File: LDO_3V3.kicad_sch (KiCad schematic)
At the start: 7 parts, among them U4 TPS7A8101DRBR

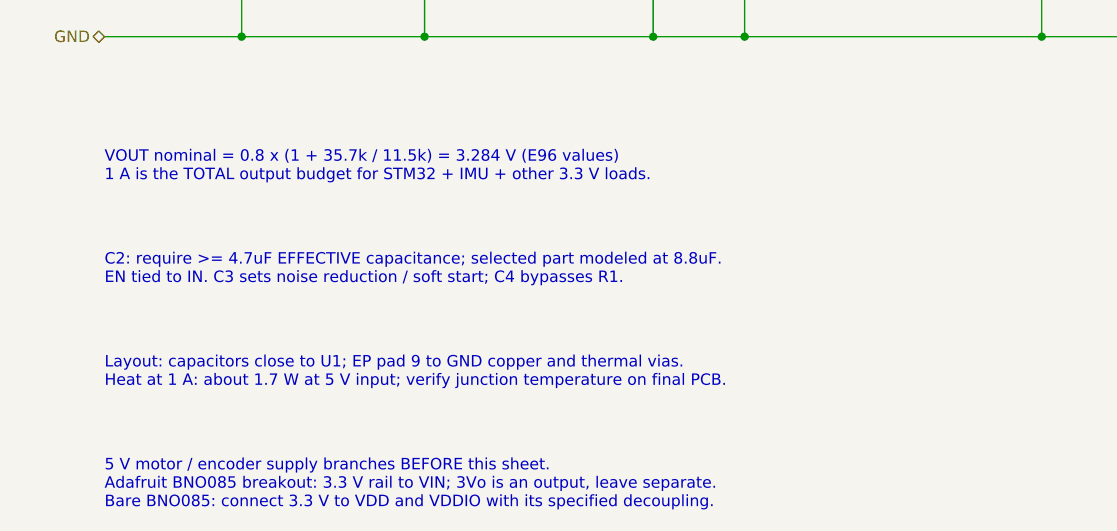
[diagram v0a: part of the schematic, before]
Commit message: Remove the IMU from the board; it will be wired off-board
The BNO085 IMU is now connected discretely off the PCB, so everything
for it is removed from the schematic and the layout:
- Delete the IMU Interface sheet (IMU_Interface.kicad_sch): J11 STEMMA
  QT connector, J12 INT/RST header, DNP I2C pull-ups R10/R11 and series
  resistors R34/R35; remove its sheet block, note and project entry
- Remove debug LED D10 / R23 (LED_IMU on PB13)
- Rename the freed MCU nets back to plain pins, still broken out on the
  GPIO headers: IMU_SCL -> PB6, IMU_SDA -> PB7 (J9), IMU_INT -> PC4,
  IMU_RST -> PC5 (J10), LED_IMU -> PB13 (J9)
- Drop IMU wiring notes and the IMU 3.3 V budget line from the LDO sheet;
  update the J9/J10 pin descriptions, debug-LED note and README

Board updated to match (as Update PCB from Schematic): the eight
unplaced footprints deleted, pad nets renamed, J9/J10 descriptions
synced. ERC 0; DRC unchanged at 57 with 276 unrouted (was 293);
schematic parity clean.

Co-Authored-By: Claude Opus 5.5 <noreply@anthropic.com>
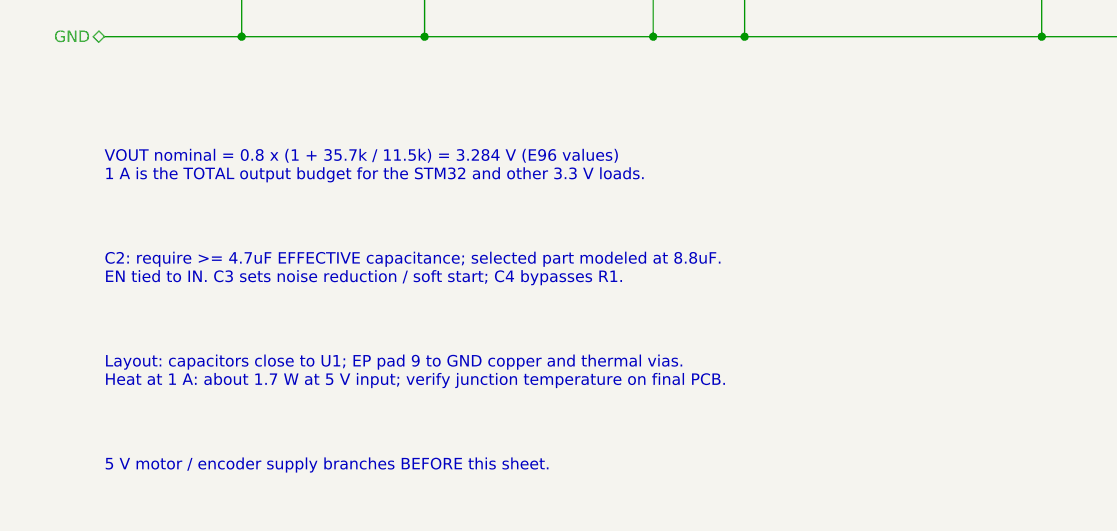
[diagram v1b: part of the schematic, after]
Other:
- note added: "5 V motor / encoder supply branches BEFORE this sheet."
- note added: "VOUT nominal = 0.8 x (1 + 35.7k / 11.5k) = 3.284 V (E96 values) 1 A is the TOTAL output budget for the STM32 and other 3.3 V loads."
- note removed: "5 V motor / encoder supply branches BEFORE this sheet. Adafruit BNO085 breakout: 3.3 V rail to VIN; 3Vo is an output, leave separate. Bare BNO085: connect 3.3 V to VDD and VDDIO with its specified decoupling."
- note removed: "VOUT nominal = 0.8 x (1 + 35.7k / 11.5k) = 3.284 V (E96 values) 1 A is the TOTAL output budget for STM32 + IMU + other 3.3 V loads."
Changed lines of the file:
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@@
 		(comment 1 "5 V to 3.3 V, 1 A total rail capacity")
 	)
-	(text "VOUT nominal = 0.8 x (1 + 35.7k / 11.5k) = 3.284 V (E96 values)\n1 A is the TOTAL output budget for STM32 + IMU + other 3.3 V loads."
+	(text "VOUT nominal = 0.8 x (1 + 35.7k / 11.5k) = 3.284 V (E96 values)\n1 A is the TOTAL output budget for the STM32 and other 3.3 V loads."
 		(exclude_from_sim no)
 		(at 60.96 144.78 0)
@@
 		)
 	)
-	(text "5 V motor / encoder supply branches BEFORE this sheet.\nAdafruit BNO085 breakout: 3.3 V rail to VIN; 3Vo is an output, leave separate.\nBare BNO085: connect 3.3 V to VDD and VDDIO with its specified decoupling."
+	(text "5 V motor / encoder supply branches BEFORE this sheet."
 		(exclude_from_sim no)
 		(at 60.96 179.07 0)

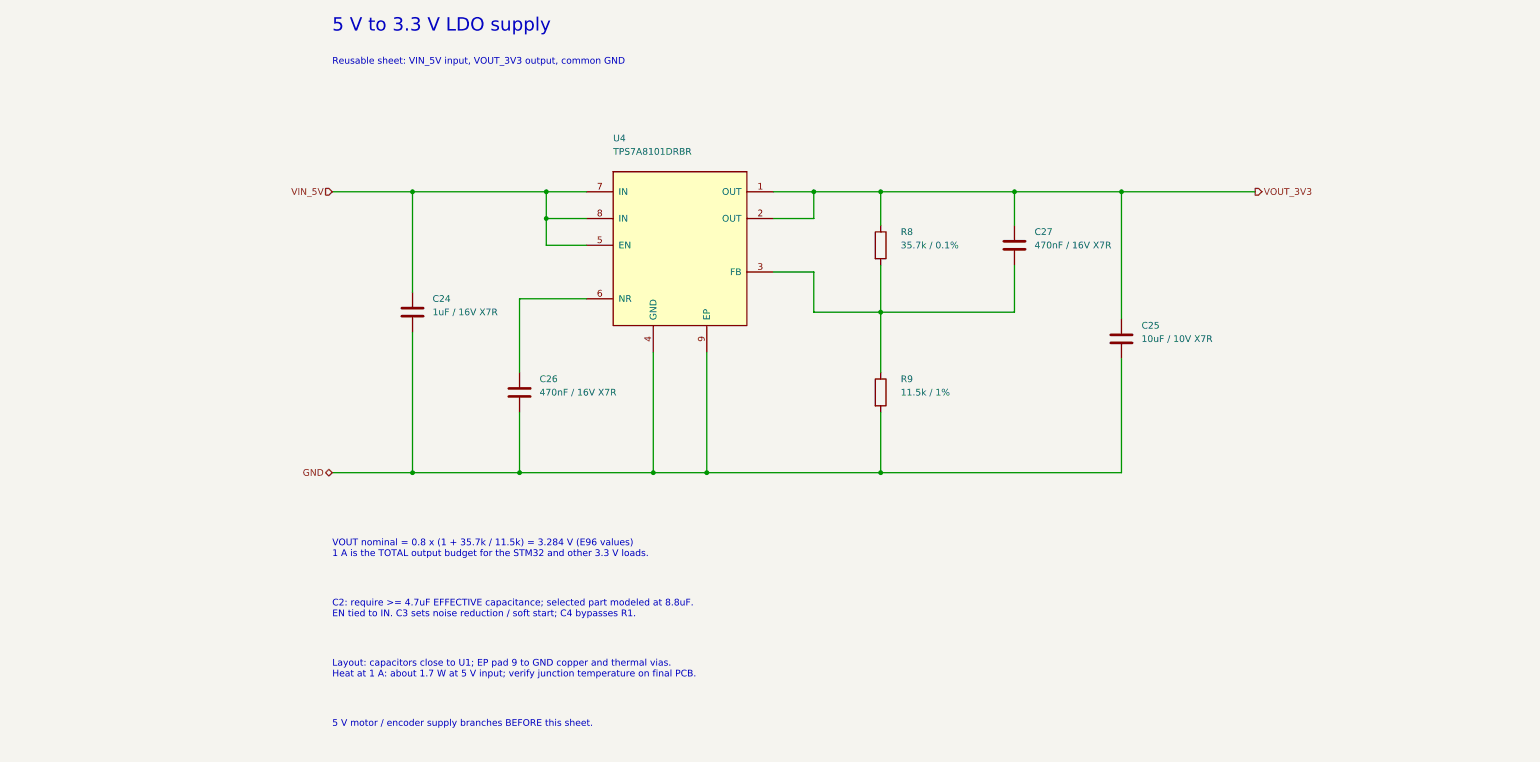
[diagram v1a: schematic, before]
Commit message: Add input protection, AUX ports, servo interface and Pi control
Implements the 2026-10-15 design review decisions in the schematic.
ERC 0 errors, 0 warnings.

New sheets:
- Input Protection: Q1 SQJ409EP reverse-battery P-FET after F1 (D12
  12 V gate clamp, R36), D13 SMBJ16A TVS on +12V, battery sense
  R37/R38/C37 -> VBAT_SENSE on PA0. PWR_FLAG moves to +12V.
- AUX Outputs: four +5V_AUX ports J18-J21 (JST XH 2-pin: Notecard,
  LiDAR, GNSS, IMU), each through a 1.5 A PTC (F4-F7).
- Servo Interface: J17 (GND, VBAT_SERVO via F3 5 A fuse, SERVO_SIG) for
  the Hiwonder HTS-30HS through an external 11.1-12 V buck. U8
  SN74LVC1T45 translates PB10 (USART3 half-duplex) to the 5 V bus,
  PB11 sets direction; R39-R42 pull-ups/series, D14 ESD.

Root sheet:
- F1 output is now VBAT_FUSED; C36 sits on +12V after Q1. J2-F1 net
  named VBAT_IN. F1 7.5 A -> 10 A (0297010.L).
- Y3/C5/C6 fitted (were DNP).
- PA0 -> VBAT_SENSE, PA1 -> PI_3V3_SENSE, PB10 -> SERVO_TX,
  PB11 -> SERVO_DIR. Notes updated (no more F2 / XT30-only text).

Pi 5 Interface:
- J13 -> 6-pin JST XH: TXD, RXD, GND, PI_3V3, PI_RESET, PI_BOOT0.
- PI_3V3 -> D15 -> AUX_EN (U5 enable) and R44/R45 -> PA1.
- PI_RESET -> Q2 DMN63D8L -> NRST (open drain, R46 pull-down).
- PI_BOOT0 -> R47 1k -> BOOT0, for reflashing over USART2.
- R12/R13 100R -> 1k (PA2/PA3 are TTa, 5 mA injection max).
- Remove TP2 (same net as TP1 since F2 was removed).

Buck 5V AUX: U5 EN from AUX_EN (was +12V), R43 100k pull-down, C40,
J22 force-on jumper. Buck 5V SYS: C49 100 nF at U3 VIN/GND.
U2/U5 value TPSM63606RDLR; VCC design note corrected (internal 1 uF,
must stay NC).

Motor Control (now A3):
- U9/U10 74LVC2G17 encoder buffers on +3V3; encoder series R 100R ->
  1k with C43-C46 1 nF; R48-R51 4.7k pull-ups (DNP).
- F8/F9 0.2 A PTC + C47/C48 on each encoder supply (ENC1_5V, ENC2_5V).
- J7/J15 pin order 5V, GND, A, B (matches the am-3651 plug).
- R52/R53 10k pull-downs on both PWM lines (MDD20A brakes on low).
- F10/F11 PTC in series with J6/J16 p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
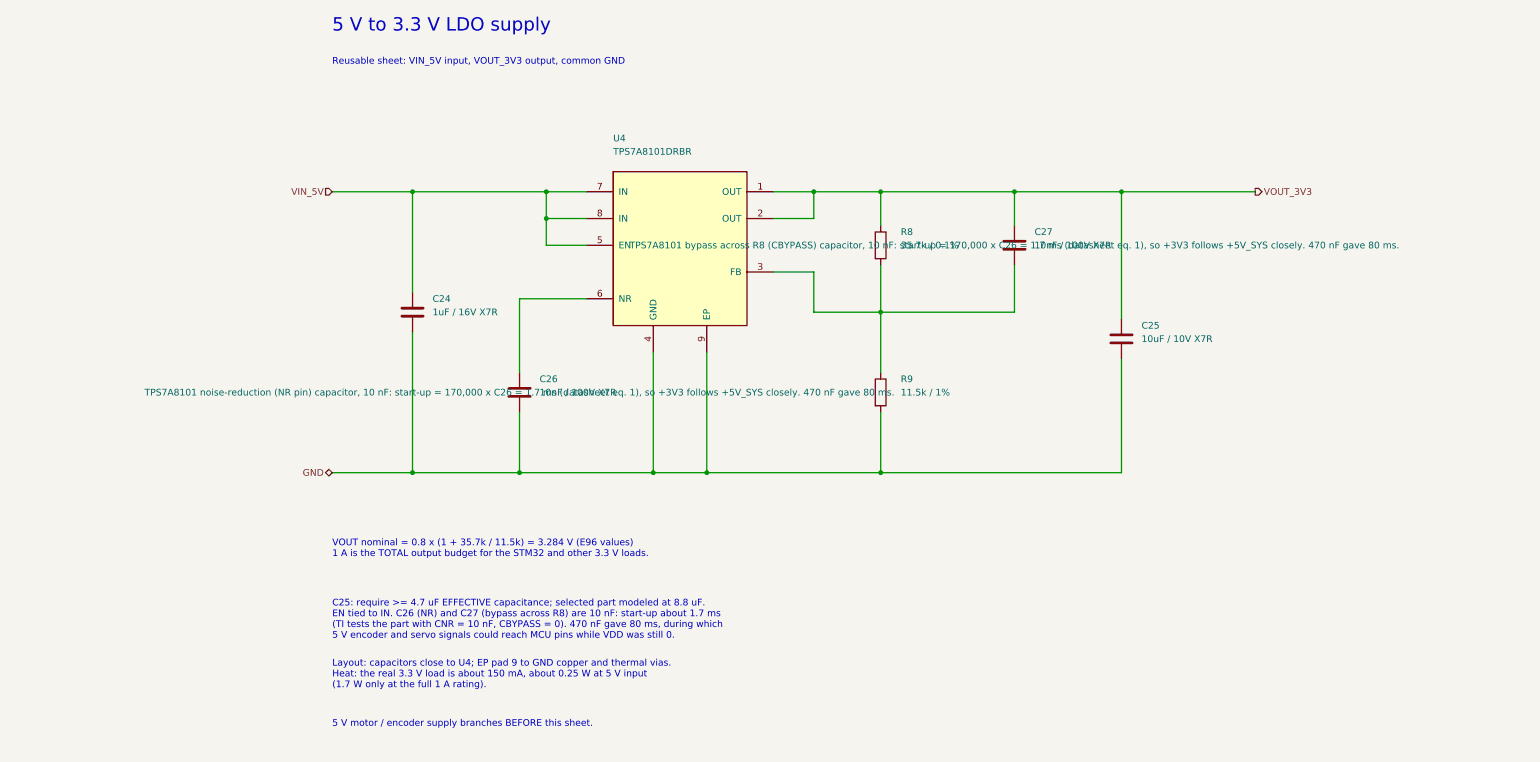
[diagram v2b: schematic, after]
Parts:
- C26, C27: value 470nF / 16V X7R -> 10nF / 100V X7R; MPN GRM188R71C474KA88D -> GRM188R72A103KA01D
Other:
- note added: "C25: require >= 4.7 uF EFFECTIVE capacitance; selected part modeled at 8.8 uF. EN tied to IN. C26 (NR) and C27 (bypass across R8) are 10 nF: start-up about 1.7 ms (TI tests the part with CNR = 10 nF, CBYPASS = 0). 470 nF gave 80 ms, during which 5 V encoder and servo signals could reach MCU pins while VDD was still 0."
- note added: "Layout: capacitors close to U4; EP pad 9 to GND copper and thermal vias. Heat: the real 3.3 V load is about 150 mA, about 0.25 W at 5 V input (1.7 W only at the full 1 A rating)."
- note removed: "C2: require >= 4.7uF EFFECTIVE capacitance; selected part modeled at 8.8uF. EN tied to IN. C3 sets noise reduction / soft start; C4 bypasses R1."
- note removed: "Layout: capacitors close to U1; EP pad 9 to GND copper and thermal vias. Heat at 1 A: about 1.7 W at 5 V input; verify junction temperature on final PCB."
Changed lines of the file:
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@@
 		)
 	)
-	(text "C2: require >= 4.7uF EFFECTIVE capacitance; selected part modeled at 8.8uF.\nEN tied to IN. C3 sets noise reduction / soft start; C4 bypasses R1."
+	(text "C25: require >= 4.7 uF EFFECTIVE capacitance; selected part modeled at 8.8 uF.\nEN tied to IN. C26 (NR) and C27 (bypass across R8) are 10 nF: start-up about 1.7 ms\n(TI tests the part with CNR = 10 nF, CBYPASS = 0). 470 nF gave 80 ms, during which\n5 V encoder and servo signals could reach MCU pins while VDD was still 0."
 		(exclude_from_sim no)
 		(at 60.96 156.21 0)
@@
 		)
 	)
-	(text "Layout: capacitors close to U1; EP pad 9 to GND copper and thermal vias.\nHeat at 1 A: about 1.7 W at 5 V input; verify junction temperature on final PCB."
+	(text "Layout: capacitors close to U4; EP pad 9 to GND copper and thermal vias.\nHeat: the real 3.3 V load is about 150 mA, about 0.25 W at 5 V input\n(1.7 W only at the full 1 A rating)."
 		(exclude_from_sim no)
 		(at 60.96 167.64 0)
@@
 			)
 		)
-		(property "Value" "470nF / 16V X7R"
+		(property "Value" "10nF / 100V X7R"
 			(at 100.33 116.84 0)
 			(show_name no)
@@
 			)
 		)
-		(property "Datasheet" "https://search.murata.co.jp/Ceramy/image/img/A01X/G101/ENG/GRM188R71C474KA88-01A.pdf"
+		(property "Datasheet" ""
 			(at 96.52 116.84 0)
 			(hide yes)
@@
 			)
 		)
-		(property "Description" ""
+		(property "Description" "TPS7A8101 noise-reduction (NR pin) capacitor, 10 nF: start-up = 170,000 x C26 = 1.7 ms (datasheet eq. 1), so +3V3 follows +5V_SYS closely. 470 nF gave 80 ms."
 			(at 96.52 116.84 0)
 			(show_name no)
@@
 			)
 		)
-		(property "MPN" "GRM188R71C474KA88D"
+		(property "MPN" "GRM188R72A103KA01D"
 			(at 96.52 116.84 0)
 			(hide yes)
@@
 			)
 		)
-		(property "Value" "470nF / 16V X7R"
+		(property "Value" "10nF / 100V X7R"
 			(at 194.31 88.9 0)
 			(show_name no)
@@
 			)
 		)
-		(property "Datasheet" "https://search.murata.co.jp/Ceramy/image/img/A01X/G101/ENG/GRM188R71C474KA88-01A.pdf"
+		(property "Datasheet" ""
 			(at 190.5 88.9 0)
 			(hide yes)
@@
 			)
 		)
-		(property "Description" ""
+		(property "Description" "TPS7A8101 bypass across R8 (CBYPASS) capacitor, 10 nF: start-up = 170,000 x C26 = 1.7 ms (datasheet eq. 1), so +3V3 follows +5V_SYS closely. 470 nF gave 80 ms."
 			(at 190.5 88.9 0)
 			(show_name no)
@@
 			)
 		)
-		(property "MPN" "GRM188R71C474KA88D"
+		(property "MPN" "GRM188R72A103KA01D"
 			(at 190.5 88.9 0)
 			(hide yes)
